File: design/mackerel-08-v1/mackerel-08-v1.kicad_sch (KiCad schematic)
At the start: 82 parts, among them J1 Conn_02x04_Counter_Clockwise, J10 Conn_02x04_Counter_Clockwise, J2 DC_Jack, J3 Conn_02x20_Counter_Clockwise, J4 Conn_02x20_Counter_Clockwise, J5 DB9_Male_MountingHoles, J6 DB9_Male_MountingHoles, J8 Conn_01x03, J9 Conn_02x04_Counter_Clockwise, SW1 SW_Push, SW2 SW_SPDT, U1 MC68008, U10 XR68C681, U11 74HC595, U12 ATF22V10C, U13 MAX3232, U14 ATF22V10C, U15 NE555P, U16 MAX3232, U17 ATF22V10C, U2 AS6C4008-55PCN, U3 AS6C4008-55PCN, U4 AS6C4008-55PCN, U5 AS6C4008-55PCN, U6 AS6C4008-55PCN, U7 AS6C4008-55PCN, U8 AS6C4008-55PCN, U9 SST39SF040, X1 CXO_DIP8, X2 CXO_DIP8

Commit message: SPI and DUART schematic work, Rough sketch of Mackerel-30
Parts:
- removed C1: C_Polarized, Capacitor_THT:CP_Radial_D5.0mm_P2.50mm, symbol Device:C_Polarized
- removed C10, C11, C12, C13, C14, C15, C16, C17, C18, C19, C29, C3, C30, C4, C5, C6, C7, C8, C9: C, Capacitor_THT:C_Disc_D4.3mm_W1.9mm_P5.00mm, symbol Device:C
- removed C2: C_Polarized, Capacitor_THT:CP_Radial_D10.0mm_P5.00mm, symbol Device:C_Polarized
- removed C20, C21, C22, C23, C24, C25, C26, C27: C_Polarized_US, Capacitor_THT:CP_Radial_D5.0mm_P2.50mm, symbol Device:C_Polarized_US
- removed D1, D2, D3: LED, LED_THT:LED_D5.0mm, symbol Device:LED
- removed J1, J10, J9: Conn_02x04_Counter_Clockwise, Connector_PinSocket_2.54mm:PinSocket_2x04_P2.54mm_Vertical, symbol Connector_Generic:Conn_02x04_Counter_Clockwise
- removed J2: DC_Jack, Connector_BarrelJack:BarrelJack_GCT_DCJ200-10-A_Horizontal, symbol mackerel-68k-symbols:DC_Jack
- removed J3, J4: Conn_02x20_Counter_Clockwise, Connector_IDC:IDC-Header_2x20_P2.54mm_Vertical, symbol Connector_Generic:Conn_02x20_Counter_Clockwise
- removed J5, J6: DB9_Male_MountingHoles, Connector_Dsub:DSUB-9_Male_Horizontal_P2.77x2.84mm_EdgePinOffset7.70mm_Housed_MountingHolesOffset9.12mm, symbol Connector:DB9_Male_MountingHoles
- removed J8: Conn_01x03, Connector_PinHeader_2.54mm:PinHeader_1x03_P2.54mm_Vertical, symbol Connector_Generic:Conn_01x03
- removed R1, R10, R11, R12, R13, R14, R15, R16, R2: R, Resistor_THT:R_Axial_DIN0207_L6.3mm_D2.5mm_P7.62mm_Horizontal, symbol Device:R
- removed SW1: SW_Push, Button_Switch_THT:SW_PUSH_6mm_H5mm, symbol Switch:SW_Push
- removed SW2: SW_SPDT, herring:SW_Mini_Toggle, symbol Switch:SW_SPDT
- removed U10: XR68C681, Package_LCC:PLCC-44_THT-Socket, symbol mackerel-68k-symbols:XR68C681
- removed U13, U16: MAX3232, Package_DIP:DIP-16_W7.62mm, symbol Interface_UART:MAX3232
- removed U15: NE555P, Package_DIP:DIP-8_W7.62mm, symbol Timer:NE555P
- removed U2, U3, U4, U5, U6, U7, U8: AS6C4008-55PCN, Package_DIP:DIP-32_W15.24mm, symbol Memory_RAM:AS6C4008-55PCN
- removed U9: SST39SF040, Socket:DIP_Socket-32_W11.9_W12.7_W15.24_W17.78_W18.5_3M_232-1285-00-0602J, symbol mackerel-68k-symbols:SST39SF040
- removed X2: CXO_DIP8, Oscillator:Oscillator_DIP-8, symbol Oscillator:CXO_DIP8
- added J3: Conn_02x20_Odd_Even, Connector_IDC:IDC-Header_2x20_P2.54mm_Vertical, symbol Connector_Generic:Conn_02x20_Odd_Even
- added J9: Conn_01x12, Connector_PinHeader_2.54mm:PinHeader_1x12_P2.54mm_Vertical, symbol Connector_Generic:Conn_01x12
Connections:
- net /DTACK0 is gone; now on net /DTACK2: U17.2 (IN1)
- net /DTACK1 is gone; now on net /AS: U17.3 (IN2)
- net /IO is gone; now on net /EXP: U12.14 (IO0)
- net +5V: now also J3.1 (Pin_1), J3.2 (Pin_2)
- net A0: now also J3.13 (Pin_13)
- net A1: now also J3.14 (Pin_14)
- net A10: now also J3.25 (Pin_25)
- net A11: now also J3.26 (Pin_26)
- net A12: now also J3.27 (Pin_27)
- net A13: now also J3.28 (Pin_28)
- net A14: now also J3.29 (Pin_29)
- net A15: now also J3.30 (Pin_30)
- net A2: now also J3.15 (Pin_15)
- net A3: now also J3.16 (Pin_16)
- net A4: now also J3.17 (Pin_17)
- net A5: now also J3.18 (Pin_18)
- net A6: now also J3.19 (Pin_19)
- net A7: now also J3.20 (Pin_20)
- net A8: now also J3.23 (Pin_23)
- net A9: now also J3.24 (Pin_24)
- net D0: now also J3.5 (Pin_5)
- net D1: now also J3.6 (Pin_6)
- net D2: now also J3.7 (Pin_7)
- net D3: now also J3.8 (Pin_8)
- net D4: now also J3.9 (Pin_9)
- net D5: now also J3.10 (Pin_10)
- net D6: now also J3.11 (Pin_11)
- net D7: now also J3.12 (Pin_12)
- net GND: now also J3.21 (Pin_21), J3.22 (Pin_22), J3.3 (Pin_3), J3.39 (Pin_39), J3.4 (Pin_4), J3.40 (Pin_40)
- net /AS: now also J3.33 (Pin_33)
- net /DS: now also U17.4 (IN3/PD), J3.34 (Pin_34)
- net /DTACK2: now also J3.37 (Pin_37); no longer U17.4 (IN3/PD)
- net /DUART: now also U17.8 (IN7)
- net /IACK: now also U17.5 (IN4)
- net /IACK2: now also U17.7 (IN6), J3.38 (Pin_38)
- net /IACK_DUART: now also U17.6 (IN5)
- net /IRQ2: now also J3.36 (Pin_36)
- net /RESET: now also J3.31 (Pin_31)
- net /RW: now also J3.32 (Pin_32)
- net /DTACK_DUART: now reaches U17.1 (CLK/IN0)
- net IN9: now reaches U17.10 (IN9)
- net IN9: now also J9.12 (Pin_12)
- net IN10: now reaches U17.11 (IN10)
- net IN10: now also J9.11 (Pin_11)
- net IN11: now reaches U17.13 (IN11)
- net IN11: now also J9.10 (Pin_10)
- net IO0: now reaches U17.14 (IO0)
- net IO0: now also J9.9 (Pin_9)
- net IO1: now reaches U17.15 (IO1)
- net IO1: now also J9.8 (Pin_8)
- net IO2: now reaches U17.16 (IO2)
- net IO2: now also J9.7 (Pin_7)
- net IO3: now reaches U17.17 (IO3)
- net IO3: now also J9.6 (Pin_6)
- net IO4: now reaches U17.18 (IO4)
- net IO4: now also J9.5 (Pin_5)
- net IO5: now reaches U17.19 (IO5)
- net IO5: now also J9.4 (Pin_4)
- net IO6: now reaches U17.20 (IO6)
- net IO6: now also J9.3 (Pin_3)
- net IO7: now reaches U17.21 (IO7)
- net IO7: now also J9.2 (Pin_2)
- net IO8: now reaches U17.22 (IO8)
- net IO8: now also J9.1 (Pin_1)
- net /EXP: now reaches U17.9 (IN8)
- net /EXP: now also J3.35 (Pin_35)
- net /IACK3: no longer names the net of U14.17 (IO3)
- net /IACK4: no longer names the net of U14.16 (IO2)
- net /IACK5: no longer names the net of U14.15 (IO1)
- net /INT_DUART renamed /IRQ_DUART
- net /IRQ3: no longer names the net of U14.7 (IN6)
- net /IRQ4: no longer names the net of U14.8 (IN7)
- net /IRQ5: no longer names the net of U14.9 (IN8)
- no-connect marks 25 -> 11
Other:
- added sheet Mackerel-08 DUART (mackerel-08-duart.kicad_sch)
- added sheet Mackerel-08 Memory (mackerel-08-memory.kicad_sch)
- added sheet Mackerel-08 Power & Reset (mackerel-08-power-reset.kicad_sch)
- note added: "DTACK Decoder"
- note added: "Interrupt Decoder"
- note added: "Note: a lot of these pins are probably unneeded for DTACK genertion"
- note added: "Spare I/O lines on the PLD"
- note added: "TODO: SPI interrupts high or low?"
- note added: "TODO: pulldowns on unused PLD inputs"
- note added: "TODO: pullup on IRQ in lines"
- note added: "TODO: pullups on SPI int lines"
- note removed: "Power-on Reset"
- note removed: "TODO: Figure out IACK/DTACK relationship"
- note removed: "TODO: add interrupt pins"
- note removed: "TODO: check the pinout of CTS/RTS and the DB-9 connector"
- note removed: "TODO: include SPI interrupts"
- note removed: "TODO: power switch"
- note removed: "TODO: what goes into DTACK generation?"
- moved on the sheet: H1, H2, H3, H4, U12, U14, U17

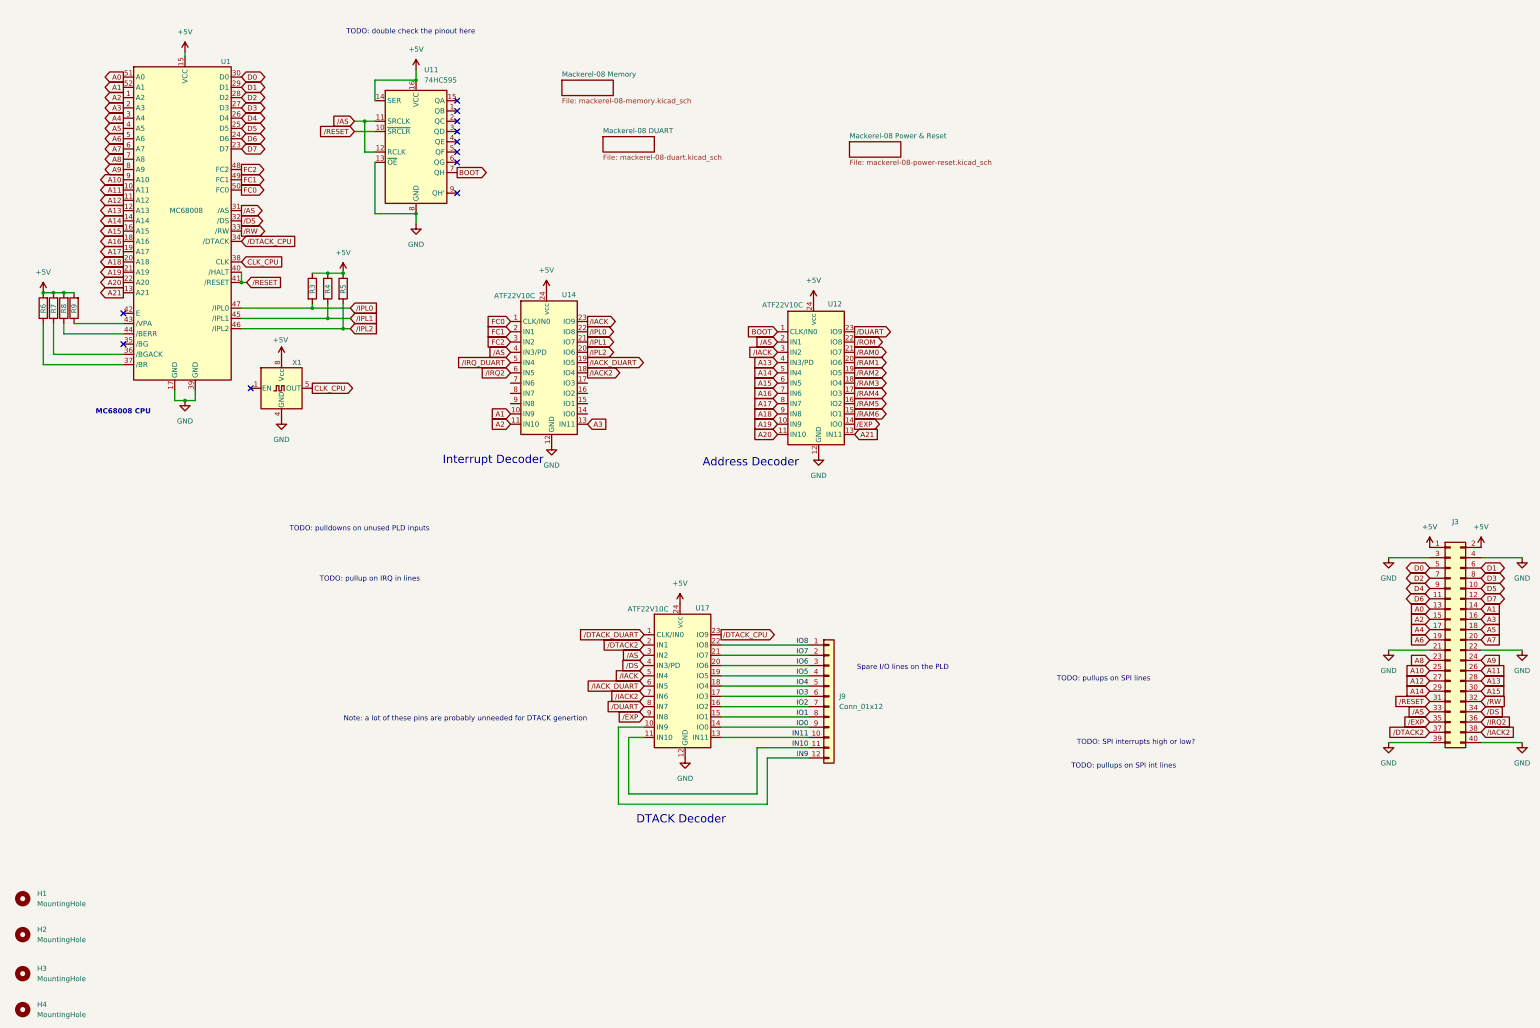
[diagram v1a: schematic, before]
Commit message: Clean up the schematic, ready for final routing
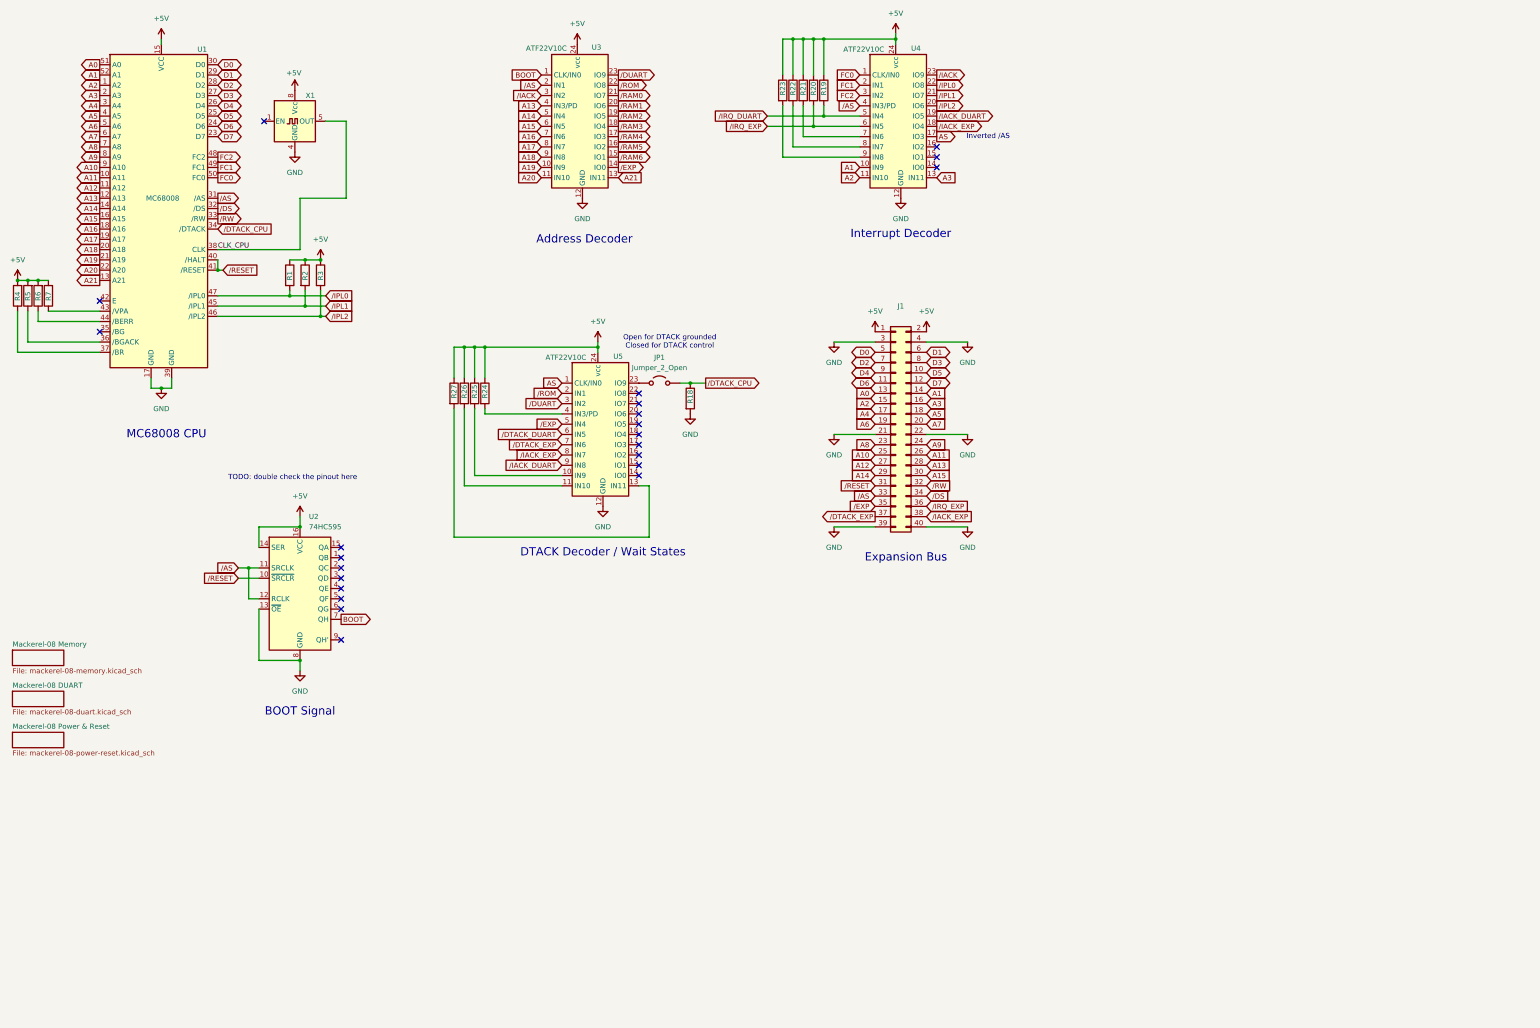
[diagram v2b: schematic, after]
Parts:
- removed H1, H2, H3, H4: MountingHole, MountingHole:MountingHole_3.2mm_M3_Pad, symbol Mechanical:MountingHole
- removed J9: Conn_01x12, Connector_PinHeader_2.54mm:PinHeader_1x12_P2.54mm_Vertical, symbol Connector_Generic:Conn_01x12
- added JP1: Jumper_2_Open, Connector_PinHeader_2.54mm:PinHeader_1x02_P2.54mm_Vertical, symbol Jumper:Jumper_2_Open
- added R18, R19, R20, R21, R22, R23, R24, R25, R26, R27: R, Resistor_THT:R_Axial_DIN0207_L6.3mm_D2.5mm_P7.62mm_Horizontal, symbol Device:R
- renumbered J3 to J1, R3 to R1, R4 to R2, R5 to R3, R6 to R4, R7 to R5, R8 to R6, R9 to R7, U11 to U2, U12 to U3, U14 to U4, U17 to U5
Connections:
- net +5V: now also R19.1, R20.1, R21.1, R22.1, R23.1, R24.1, R25.1, R26.1, R27.1
- net GND: now also R18.2
- net /AS: no longer U5.3 (IN2)
- net /DS: no longer U5.4 (IN3/PD)
- net /DTACK_CPU: now also JP1.2 (B), R18.1; no longer U5.23 (IO9)
- net /DTACK_DUART: now also U5.6 (IN5); no longer U5.1 (CLK/IN0)
- net /DUART: now also U5.3 (IN2); no longer U5.8 (IN7)
- net /EXP: now also U5.5 (IN4); no longer U5.9 (IN8)
- net /IACK: no longer U5.5 (IN4)
- net /IACK_DUART: now also U5.9 (IN8); no longer U5.6 (IN5)
- net /IRQ_DUART: now also R19.2
- net /ROM: now also U5.2 (IN1)
- net AS: now reaches U4.17 (IO3)
- net AS: now also U5.1 (CLK/IN0)
- net at U4.7 (IN6): now also R21.2
- net at U4.8 (IN7): now also R22.2
- net at U4.9 (IN8): now also R23.2
- net IN10: no longer names the net of U5.11 (IN10)
- net IN10: now also R26.2
- net IN11: no longer names the net of U5.13 (IN11)
- net IN11: now also R27.2
- net IN9: no longer names the net of U5.10 (IN9)
- net IN9: now also R25.2
- net IO0: no longer names the net of U5.14 (IO0)
- net IO1: no longer names the net of U5.15 (IO1)
- net IO2: no longer names the net of U5.16 (IO2)
- net IO3: no longer names the net of U5.17 (IO3)
- net IO4: no longer names the net of U5.18 (IO4)
- net IO5: no longer names the net of U5.19 (IO5)
- net IO6: no longer names the net of U5.20 (IO6)
- net IO7: no longer names the net of U5.21 (IO7)
- net IO8: no longer names the net of U5.22 (IO8)
- net /DTACK2 renamed /DTACK_EXP
- net /DTACK_EXP: now also U5.7 (IN6); no longer U5.2 (IN1)
- net /IACK2 renamed /IACK_EXP
- net /IACK_EXP: now also U5.8 (IN7); no longer U5.7 (IN6)
- net /IRQ2 renamed /IRQ_EXP
- net /IRQ_EXP: now also R20.2
- new net: JP1.1 (A), U5.23 (IO9)
- new net: R24.2, U5.4 (IN3/PD)
- no-connect marks 11 -> 23
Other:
- note added: "BOOT Signal"
- note added: "DTACK Decoder / Wait States"
- note added: "Expansion Bus"
- note added: "Inverted /AS"
- note added: "Open for DTACK grounded Closed for DTACK control"
- note removed: "DTACK Decoder"
- note removed: "Note: a lot of these pins are probably unneeded for DTACK genertion"
- note removed: "Spare I/O lines on the PLD"
- note removed: "TODO: SPI interrupts high or low?"
- note removed: "TODO: pulldowns on unused PLD inputs"
- note removed: "TODO: pullup on IRQ in lines"
- note removed: "TODO: pullups on SPI int lines"
- note removed: "TODO: pullups on SPI lines"
- title: Mackerel-08 v1 -> Mackerel-08 SBC v1
- moved on the sheet: J1, R1, R2, R3, R4, R5, R6, R7, U1, U2, U3, U4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

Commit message: Mackerel-08 v1 is fully routed, needs graphics, labels, and cleanup
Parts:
- removed R21, R22, R23, R24, R25, R26, R27: R, Resistor_THT:R_Axial_DIN0207_L6.3mm_D2.5mm_P7.62mm_Horizontal, symbol Device:R
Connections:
- net GND: now also U4.7 (IN6), U4.8 (IN7), U4.9 (IN8), U5.10 (IN9), U5.11 (IN10), U5.13 (IN11), U5.4 (IN3/PD)

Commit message: Mackerel-08 SVC v1 labeled and ready for final checks
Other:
- note removed: "TODO: double check the pinout here"
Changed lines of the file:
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@@
-		)
-	)
-	(text "TODO: double check the pinout here"
-		(exclude_from_sim no)
-		(at 69.85 129.54 0)
-		(effects
-			(font
-				(size 1.27 1.27)
-			)
-			(justify left bottom)
 		)
 	)
